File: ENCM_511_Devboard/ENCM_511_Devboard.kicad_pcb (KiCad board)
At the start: 2 copper layers, 23 parts, among them J1 Barrel_Jack_MountingPin, J2 Conn_01x05_Socket, J3 Conn_01x05_Socket, J4 Conn_01x16_Socket, J5 Conn_01x04_Socket, J6 Conn_01x04_Socket, SW1 SW_Push, SW2 SW_Push, SW3 SW_Push, SW4 SW_Push, U1 LM1117DT-3.3, U2 PIC24FJ256GA702-I/SO

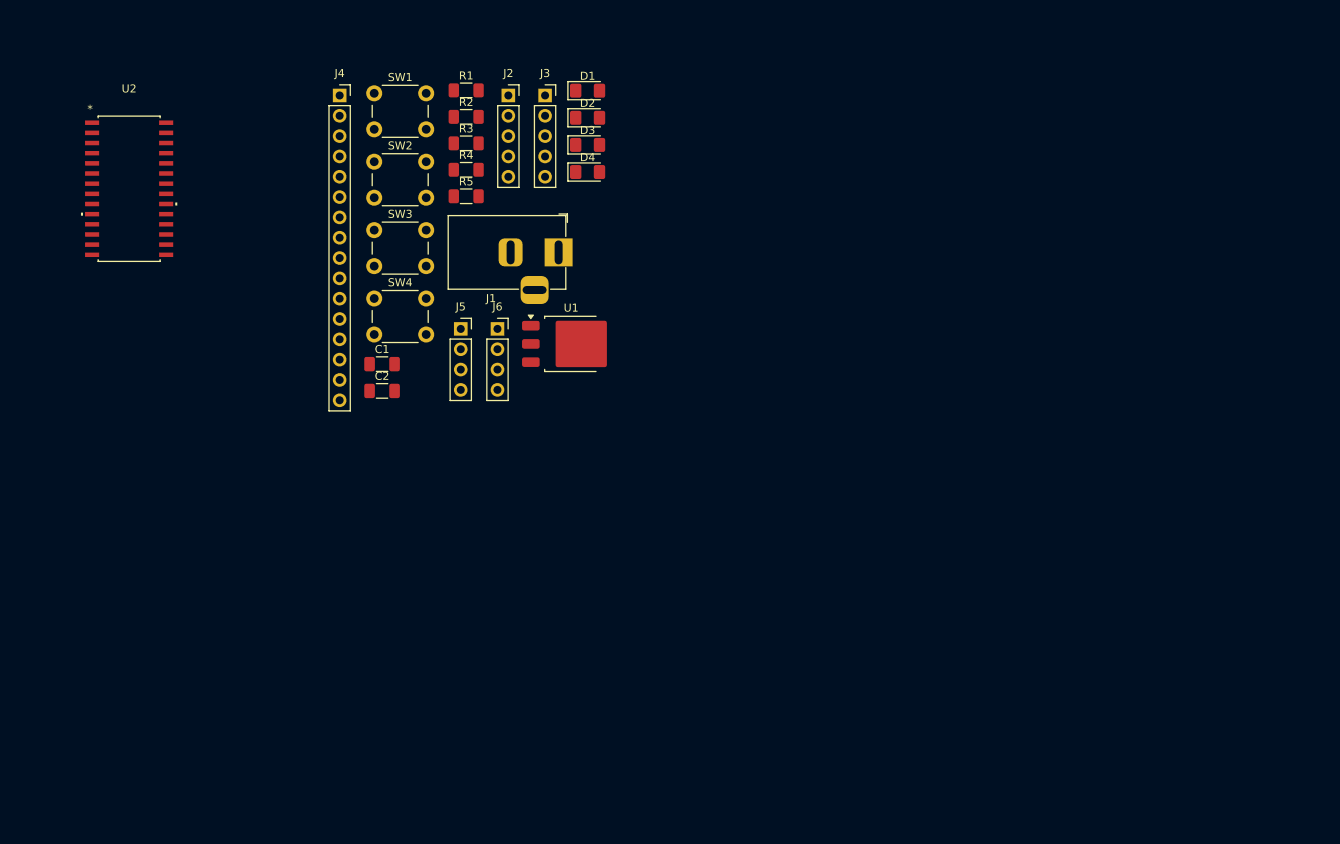
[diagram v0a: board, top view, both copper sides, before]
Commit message: Fixed an Issue with Debugger Connections
This is for PGD and PGC which were unconnected in the first revision.
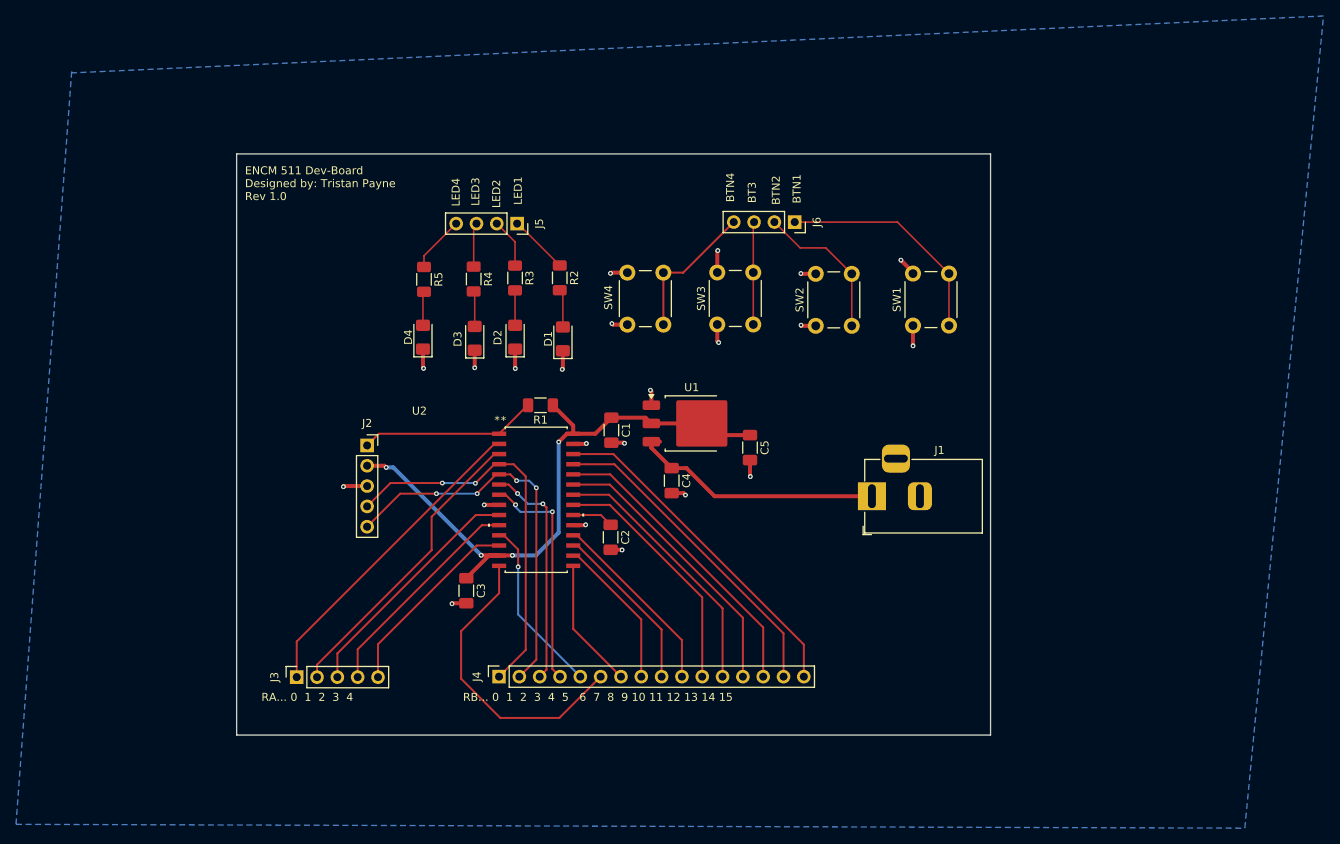
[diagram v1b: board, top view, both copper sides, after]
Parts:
- added C3: 100n, Capacitor_SMD:C_1206_3216Metric_Pad1.33x1.80mm_HandSolder, F.Cu at (97.0, 107.3)
- added C4: 10 uF, Capacitor_SMD:C_1206_3216Metric_Pad1.33x1.80mm_HandSolder, F.Cu at (122.7, 93.5)
- added C5: 10uF, Capacitor_SMD:C_1206_3216Metric_Pad1.33x1.80mm_HandSolder, F.Cu at (132.5, 89.4)
- moved J3 79.1 mm to (75.8, 118.1), turned to 90 degrees
- moved J4 75.3 mm to (101.1, 118.0), turned to 90 degrees
- moved SW1 73.3 mm to (152.8, 74.1), turned to 90 degrees
- moved U2 64.0 mm to (105.7, 95.9)
- moved SW2 58.9 mm to (140.7, 74.2), turned to 90 degrees
- moved J1 49.6 mm to (147.7, 95.4), turned to 180 degrees
- moved J2 47.2 mm to (84.6, 89.1)
- moved SW3 44.5 mm to (128.4, 74.0), turned to 90 degrees
- moved R1 40.4 mm to (106.3, 84.1), turned to 180 degrees
- moved J6 39.5 mm to (138.1, 61.2), turned to -90 degrees
- moved C2 33.9 mm to (115.0, 100.6), turned to -90 degrees
- moved SW4 31.8 mm to (117.1, 74.0), turned to 90 degrees
- moved D1 31.2 mm to (109.1, 75.8), turned to 90 degrees
- moved C1 29.8 mm to (115.1, 87.2), turned to -90 degrees
- moved D4 29.2 mm to (91.6, 75.6), turned to 90 degrees
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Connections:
- J2 pad 4: /PGD -> /PGD/RB0
- J2 pad 5: /PGC -> /PGC/RB1
- J4 pad 1: /RB0 -> /PGD/RB0
- J4 pad 2: /RB1 -> /PGC/RB1
- U2 pad 4: /RB0 -> /PGD/RB0
- U2 pad 5: /RB1 -> /PGC/RB1
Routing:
- net +3.3V: track 0.00 -> 77.7 mm, vias 0 -> 4
- net /PGC/RB1: track 0.00 -> 49.7 mm, vias 0 -> 4
- net /PGD/RB0: track 0.00 -> 49.1 mm, vias 0 -> 2
- net GND: track 0.00 -> 46.1 mm, vias 0 -> 22
- net /RB15: track 0.00 -> 42.7 mm
- net /RB14: track 0.00 -> 40.5 mm
- net /RA0: track 0.00 -> 40.0 mm
- net /RB13: track 0.00 -> 37.8 mm
- net /RB5: track 0.00 -> 37.7 mm
- net /RA1: track 0.00 -> 37.7 mm
- net /RB12: track 0.00 -> 35.5 mm
- net /RB11: track 0.00 -> 33.1 mm
- net +5V: track 0.00 -> 31.9 mm
- net /RB10: track 0.00 -> 30.8 mm
- net /RA2: track 0.00 -> 30.3 mm
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- added copper zone on B.Cu, net GND
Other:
- board outline added: 94.2 x 72.6 mm
- board text added: "BT3"
- board text added: "BTN1"
- board text added: "BTN2"
- board text added: "BTN4"
- board text added: "ENCM 511 Dev-Board Designed by: Tristan Payne Rev 1.0"
- board text added: "LED1"
- board text added: "LED2"
- board text added: "LED3"
- board text added: "LED4"
- board text added: "RA... 0 1 2 3 4"
- board text added: "RB... 0 1 2 3 4 5 6 7 8 9 10 11 12 13 14 15"
